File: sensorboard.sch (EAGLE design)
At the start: 15 parts, among them U1 LM1117MP-3.3, U2 LM324D

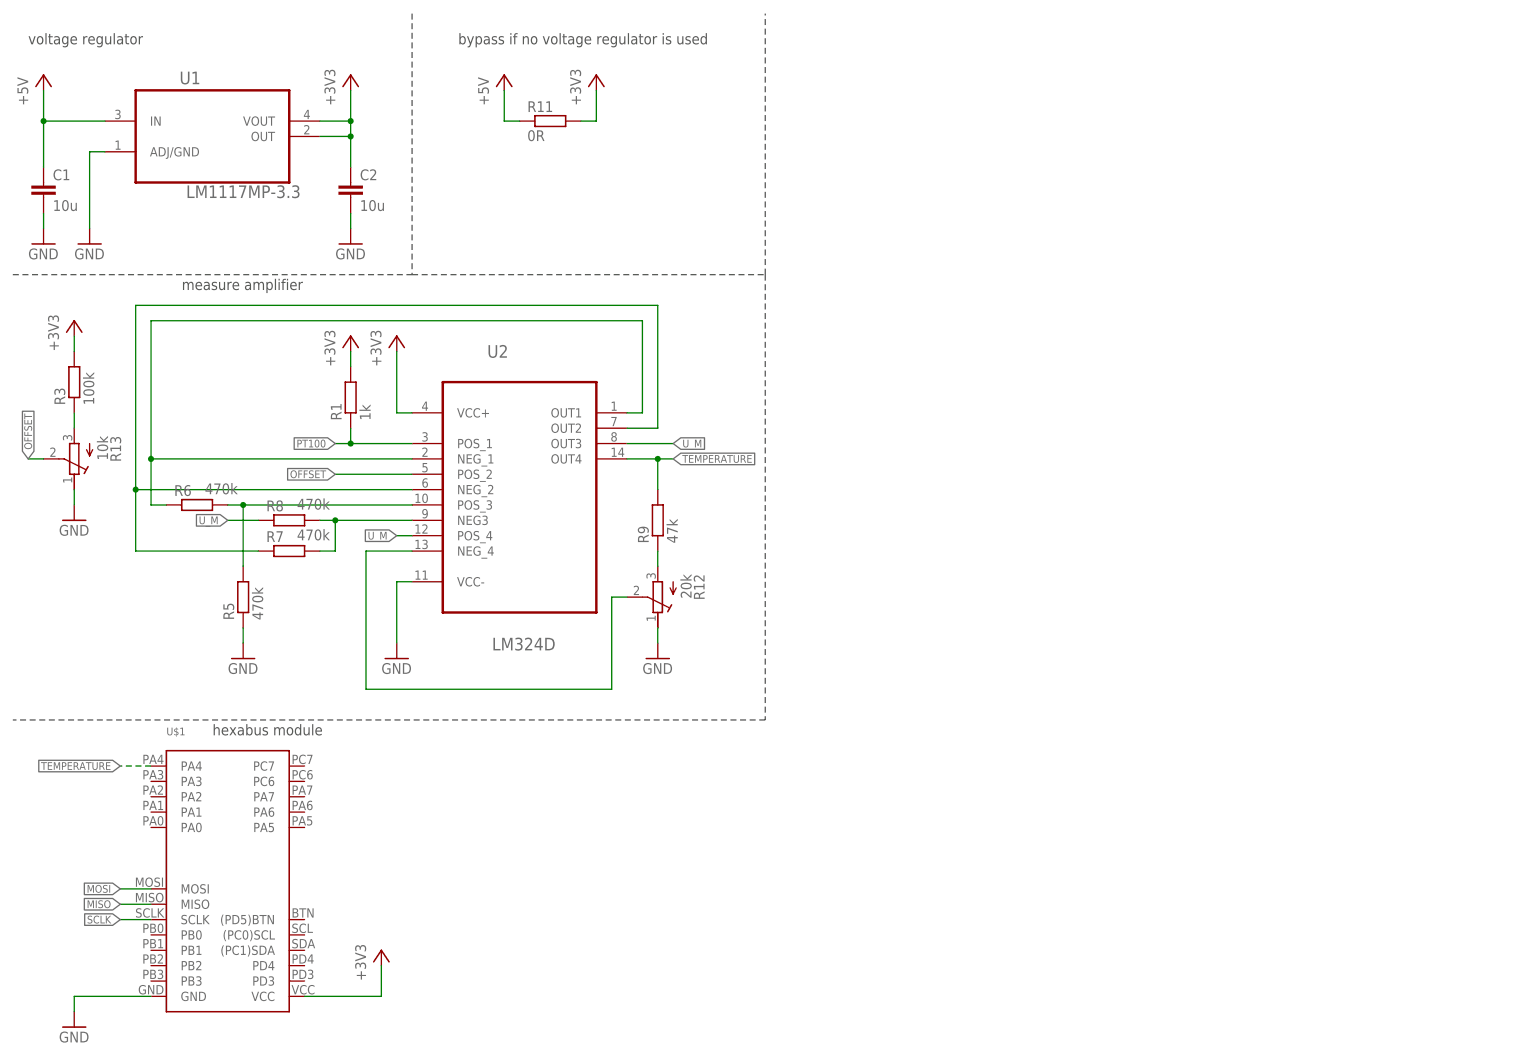
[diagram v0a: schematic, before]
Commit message: added pressure sensor
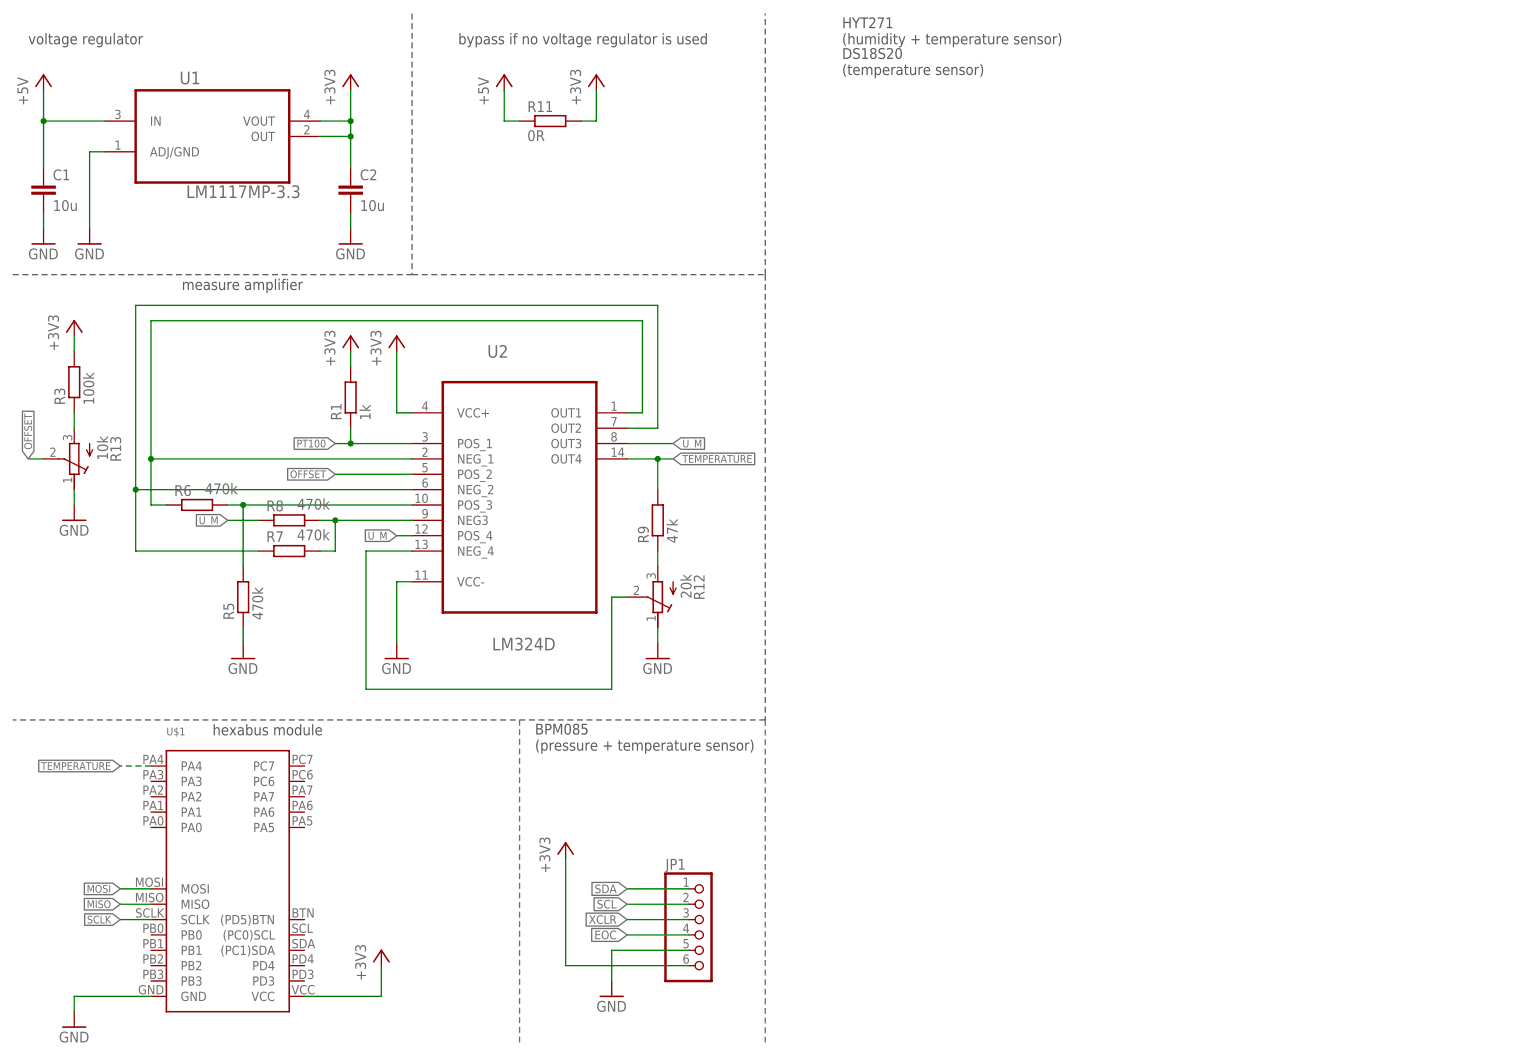
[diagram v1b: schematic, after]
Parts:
- added JP1: (no value), pinhead:PINHD-1X6
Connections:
- new net EOC: JP1.4
- new net SCL: JP1.2
- new net SDA: JP1.1
- new net XCLR: JP1.3
- net +3V3: now also JP1.6
- net GND: now also JP1.5
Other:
- note added: "BPM085 (pressure + temperature sensor)"
- note added: "DS18S20 (temperature sensor)"
- note added: "HYT271 (humidity + temperature sensor)"
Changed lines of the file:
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@@
 <part name="+3V6" library="supply1" deviceset="+3V3" device=""/>
 <part name="GND8" library="supply1" deviceset="GND" device=""/>
+<part name="JP1" library="pinhead" deviceset="PINHD-1X6" device=""/>
+<part name="GND9" library="supply1" deviceset="GND" device=""/>
+<part name="+3V7" library="supply1" deviceset="+3V3" device=""/>
 </parts>
 <sheets>
@@
 <wire x1="129.54" y1="132.08" x2="129.54" y2="58.42" width="0.1524" layer="97" style="longdash"/>
 <wire x1="129.54" y1="58.42" x2="5.08" y2="58.42" width="0.1524" layer="97" style="longdash"/>
+<text x="142.24" y="170.18" size="1.778" layer="97">HYT271
+(humidity + temperature sensor)</text>
+<text x="142.24" y="165.1" size="1.778" layer="97">DS18S20
+(temperature sensor)</text>
+<text x="91.44" y="53.34" size="1.778" layer="97">BPM085
+(pressure + temperature sensor)</text>
+<wire x1="88.9" y1="5.08" x2="88.9" y2="58.42" width="0.1524" layer="95" style="longdash"/>
+<wire x1="129.54" y1="58.42" x2="129.54" y2="5.08" width="0.1524" layer="95" style="longdash"/>
 </plain>
 <instances>
@@
 <instance part="+3V6" gate="G$1" x="15.24" y="124.46"/>
 <instance part="GND8" gate="1" x="15.24" y="91.44"/>
+<instance part="JP1" gate="A" x="119.38" y="22.86"/>
+<instance part="GND9" gate="1" x="104.14" y="12.7"/>
+<instance part="+3V7" gate="G$1" x="96.52" y="38.1"/>
 </instances>
 <busses>
@@
 <pinref part="GND8" gate="1" pin="GND"/>
 <wire x1="15.24" y1="96.52" x2="15.24" y2="93.98" width="0.1524" layer="91"/>
+</segment>
+<segment>
+<pinref part="JP1" gate="A" pin="5"/>
+<pinref part="GND9" gate="1" pin="GND"/>
+<wire x1="116.84" y1="20.32" x2="104.14" y2="20.32" width="0.1524" layer="91"/>
+<wire x1="104.14" y1="20.32" x2="104.14" y2="15.24" width="0.1524" layer="91"/>
 </segment>
 </net>
@@
 <wire x1="66.04" y1="12.7" x2="53.34" y2="12.7" width="0.1524" layer="91"/>
 </segment>
+<segment>
+<pinref part="JP1" gate="A" pin="6"/>
+<pinref part="+3V7" gate="G$1" pin="+3V3"/>
+<wire x1="116.84" y1="17.78" x2="96.52" y2="17.78" width="0.1524" layer="91"/>
+<wire x1="96.52" y1="17.78" x2="96.52" y2="35.56" width="0.1524" layer="91"/>
+</segment>
 </net>
 <net name="+5V" class="0">
@@
 </segment>
 </net>
+<net name="SDA" class="0">
+<segment>
+<pinref part="JP1" gate="A" pin="1"/>
+<wire x1="116.84" y1="30.48" x2="106.68" y2="30.48" width="0.1524" layer="91"/>
+<label x="106.68" y="30.48" size="1.4224" layer="95" rot="R180" xref="yes"/>
+</segment>
+</net>
+<net name="SCL" class="0">
+<segment>
+<pinref part="JP1" gate="A" pin="2"/>
+<wire x1="116.84" y1="27.94" x2="106.68" y2="27.94" width="0.1524" layer="91"/>
+<label x="106.68" y="27.94" size="1.4224" layer="95" rot="R180" xref="yes"/>
+</segment>
+</net>
+<net name="XCLR" class="0">
+<segment>
+<pinref part="JP1" gate="A" pin="3"/>
+<wire x1="116.84" y1="25.4" x2="106.68" y2="25.4" width="0.1524" layer="91"/>
+<label x="106.68" y="25.4" size="1.4224" layer="95" rot="R180" xref="yes"/>
+</segment>
+</net>
+<net name="EOC" class="0">
+<segment>
+<pinref part="JP1" gate="A" pin="4"/>
+<wire x1="116.84" y1="22.86" x2="106.68" y2="22.86" width="0.1524" layer="91"/>
+<label x="106.68" y="22.86" size="1.4224" layer="95" rot="R180" xref="yes"/>
+</segment>
+</net>
 </nets>
 </sheet>
@@
 </schematic>
 </drawing>
+<compatibility>
+<note version="6.3" minversion="6.2.2" severity="warning">
+Since Version 6.2.2 text objects can contain more than one line,
+which will not be processed correctly with this version.
+</note>
+</compatibility>
 </eagle>

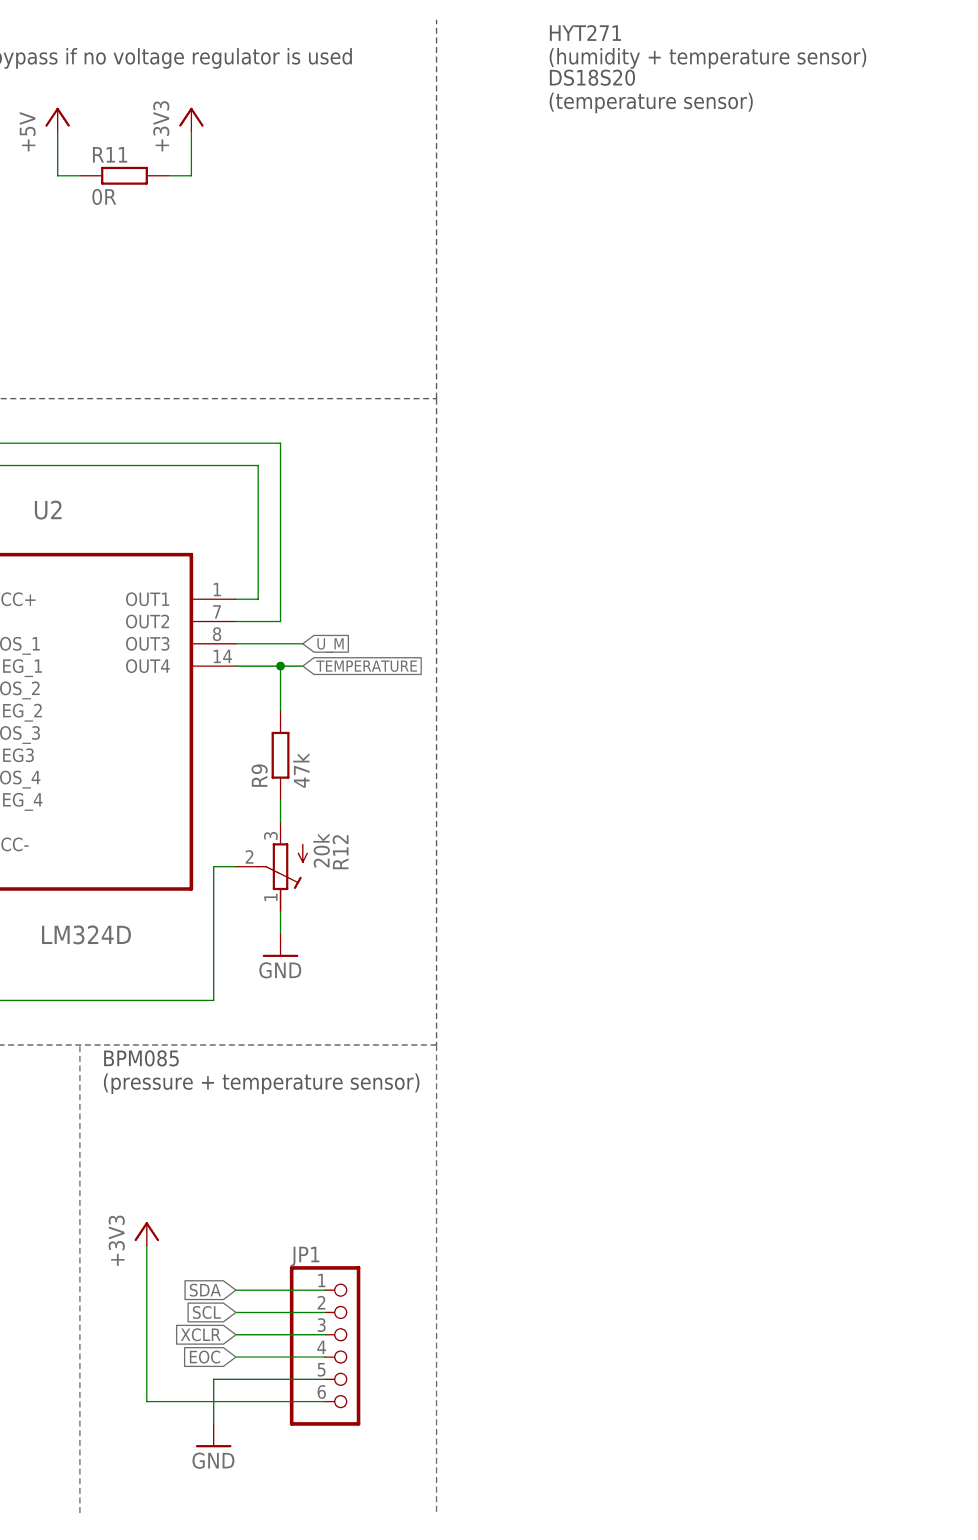
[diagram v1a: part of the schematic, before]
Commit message: added DS18S20
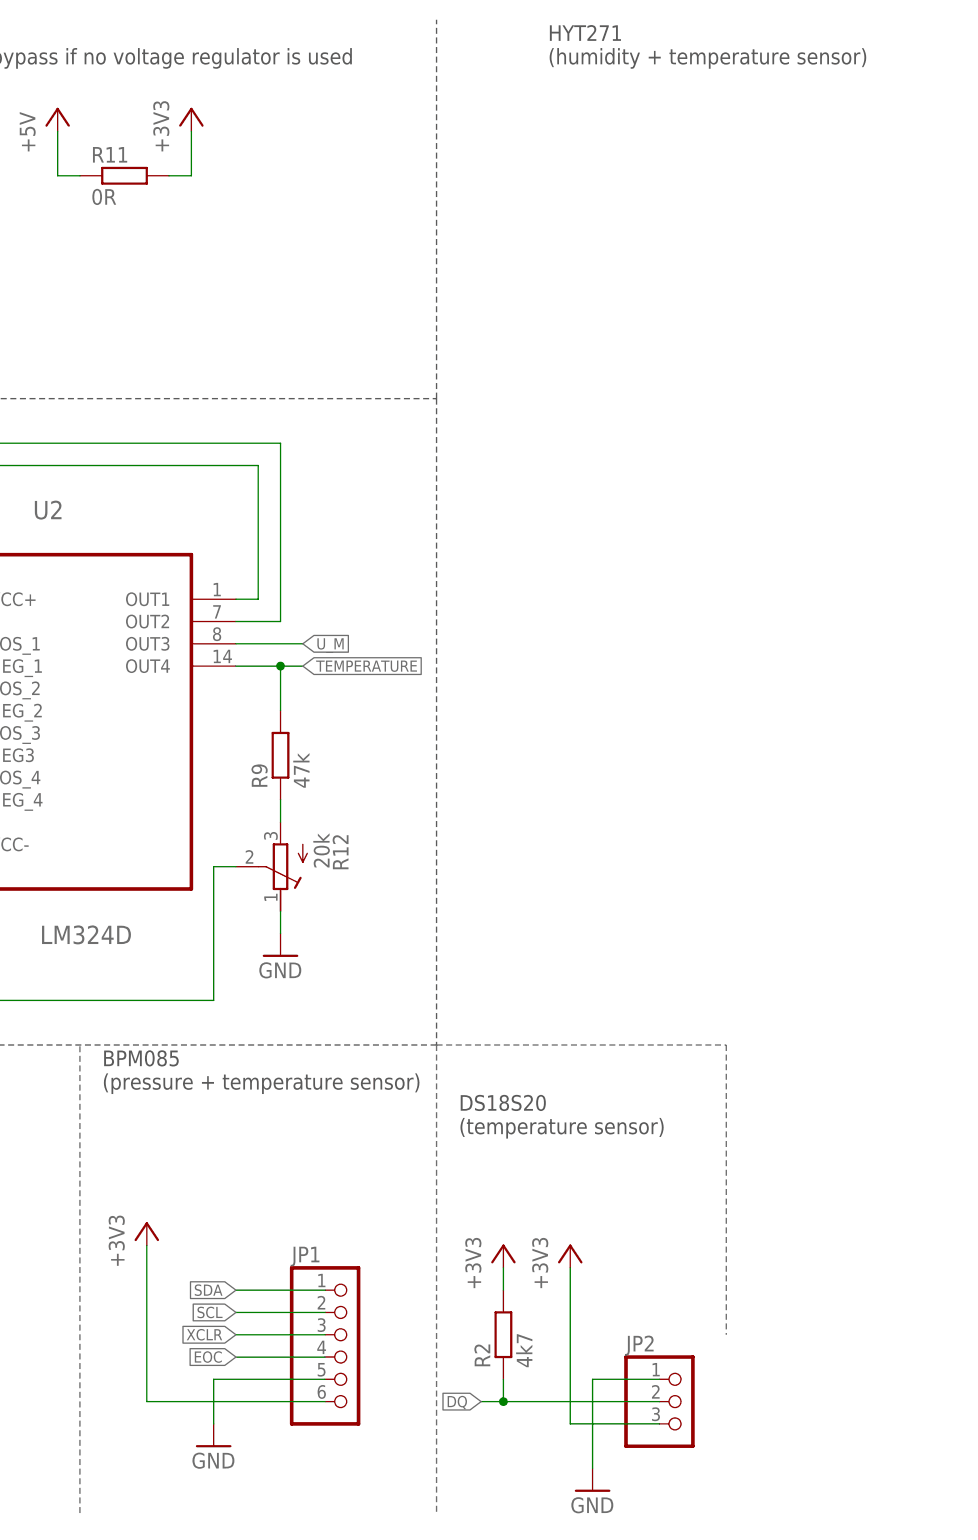
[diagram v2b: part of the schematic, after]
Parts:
- added JP2: (no value), pinhead:PINHD-1X3
- added R2: 4k7, rcl:R-EU_R0805
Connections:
- new net DQ: JP2.2, R2.1
- net +3V3: now also JP2.3, R2.2
- net GND: now also JP2.1
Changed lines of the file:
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@@
 <part name="GND9" library="supply1" deviceset="GND" device=""/>
 <part name="+3V7" library="supply1" deviceset="+3V3" device=""/>
+<part name="JP2" library="pinhead" deviceset="PINHD-1X3" device=""/>
+<part name="R2" library="rcl" deviceset="R-EU_" device="R0805" value="4k7"/>
+<part name="+3V8" library="supply1" deviceset="+3V3" device=""/>
+<part name="GND11" library="supply1" deviceset="GND" device=""/>
+<part name="+3V9" library="supply1" deviceset="+3V3" device=""/>
 </parts>
 <sheets>
@@
 <text x="142.24" y="170.18" size="1.778" layer="97">HYT271
 (humidity + temperature sensor)</text>
-<text x="142.24" y="165.1" size="1.778" layer="97">DS18S20
+<text x="132.08" y="48.26" size="1.778" layer="97">DS18S20
 (temperature sensor)</text>
 <text x="91.44" y="53.34" size="1.778" layer="97">BPM085
@@
 <wire x1="88.9" y1="5.08" x2="88.9" y2="58.42" width="0.1524" layer="95" style="longdash"/>
 <wire x1="129.54" y1="58.42" x2="129.54" y2="5.08" width="0.1524" layer="95" style="longdash"/>
+<wire x1="129.54" y1="58.42" x2="162.56" y2="58.42" width="0.1524" layer="95" style="longdash"/>
+<wire x1="162.56" y1="58.42" x2="162.56" y2="25.4" width="0.1524" layer="95" style="longdash"/>
 </plain>
 <instances>
@@
 <instance part="GND9" gate="1" x="104.14" y="12.7"/>
 <instance part="+3V7" gate="G$1" x="96.52" y="38.1"/>
+<instance part="JP2" gate="A" x="157.48" y="17.78"/>
+<instance part="R2" gate="G$1" x="137.16" y="25.4" rot="R90"/>
+<instance part="+3V8" gate="G$1" x="144.78" y="35.56"/>
+<instance part="GND11" gate="1" x="147.32" y="7.62"/>
+<instance part="+3V9" gate="G$1" x="137.16" y="35.56"/>
 </instances>
 <busses>
@@
 <wire x1="116.84" y1="20.32" x2="104.14" y2="20.32" width="0.1524" layer="91"/>
 <wire x1="104.14" y1="20.32" x2="104.14" y2="15.24" width="0.1524" layer="91"/>
+</segment>
+<segment>
+<pinref part="JP2" gate="A" pin="1"/>
+<pinref part="GND11" gate="1" pin="GND"/>
+<wire x1="154.94" y1="20.32" x2="147.32" y2="20.32" width="0.1524" layer="91"/>
+<wire x1="147.32" y1="20.32" x2="147.32" y2="10.16" width="0.1524" layer="91"/>
 </segment>
 </net>
@@
 <wire x1="96.52" y1="17.78" x2="96.52" y2="35.56" width="0.1524" layer="91"/>
 </segment>
+<segment>
+<pinref part="JP2" gate="A" pin="3"/>
+<pinref part="+3V8" gate="G$1" pin="+3V3"/>
+<wire x1="154.94" y1="15.24" x2="144.78" y2="15.24" width="0.1524" layer="91"/>
+<wire x1="144.78" y1="15.24" x2="144.78" y2="33.02" width="0.1524" layer="91"/>
+</segment>
+<segment>
+<pinref part="+3V9" gate="G$1" pin="+3V3"/>
+<pinref part="R2" gate="G$1" pin="2"/>
+<wire x1="137.16" y1="33.02" x2="137.16" y2="30.48" width="0.1524" layer="91"/>
+</segment>
 </net>
 <net name="+5V" class="0">
@@
 <pinref part="JP1" gate="A" pin="1"/>
 <wire x1="116.84" y1="30.48" x2="106.68" y2="30.48" width="0.1524" layer="91"/>
-<label x="106.68" y="30.48" size="1.4224" layer="95" rot="R180" xref="yes"/>
+<label x="106.68" y="30.48" size="1.27" layer="95" rot="R180" xref="yes"/>
 </segment>
 </net>
@@
 <pinref part="JP1" gate="A" pin="2"/>
 <wire x1="116.84" y1="27.94" x2="106.68" y2="27.94" width="0.1524" layer="91"/>
-<label x="106.68" y="27.94" size="1.4224" layer="95" rot="R180" xref="yes"/>
+<label x="106.68" y="27.94" size="1.27" layer="95" rot="R180" xref="yes"/>
 </segment>
 </net>
@@
 <pinref part="JP1" gate="A" pin="3"/>
 <wire x1="116.84" y1="25.4" x2="106.68" y2="25.4" width="0.1524" layer="91"/>
-<label x="106.68" y="25.4" size="1.4224" layer="95" rot="R180" xref="yes"/>
+<label x="106.68" y="25.4" size="1.27" layer="95" rot="R180" xref="yes"/>
 </segment>
 </net>
@@
 <pinref part="JP1" gate="A" pin="4"/>
 <wire x1="116.84" y1="22.86" x2="106.68" y2="22.86" width="0.1524" layer="91"/>
-<label x="106.68" y="22.86" size="1.4224" layer="95" rot="R180" xref="yes"/>
-</segment>
-</net>
+<label x="106.68" y="22.86" size="1.27" layer="95" rot="R180" xref="yes"/>
+</segment>
+</net>
+<net name="DQ" class="0">
+<segment>
+<pinref part="JP2" gate="A" pin="2"/>
+<wire x1="154.94" y1="17.78" x2="137.16" y2="17.78" width="0.1524" layer="91"/>
+<wire x1="137.16" y1="17.78" x2="134.62" y2="17.78" width="0.1524" layer="91"/>
+<pinref part="R2" gate="G$1" pin="1"/>
+<wire x1="137.16" y1="20.32" x2="137.16" y2="17.78" width="0.1524" layer="91"/>
+<junction x="137.16" y="17.78"/>
+<label x="134.62" y="17.78" size="1.27" layer="95" rot="R180" xref="yes"/>
+</segment>
+</net>
